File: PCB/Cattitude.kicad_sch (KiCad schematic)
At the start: 15 parts, among them J1 Conn_01x08_Pin, J2 Conn_01x04_Pin, J3 Conn_01x02_Pin, J4 Conn_01x02_Pin, J5 Conn_01x03_Pin, J6 Conn_01x03_Pin, J7 Conn_01x03_Pin, J8 Conn_01x03_Pin, SW2 SW_SPDT, U1 102010551

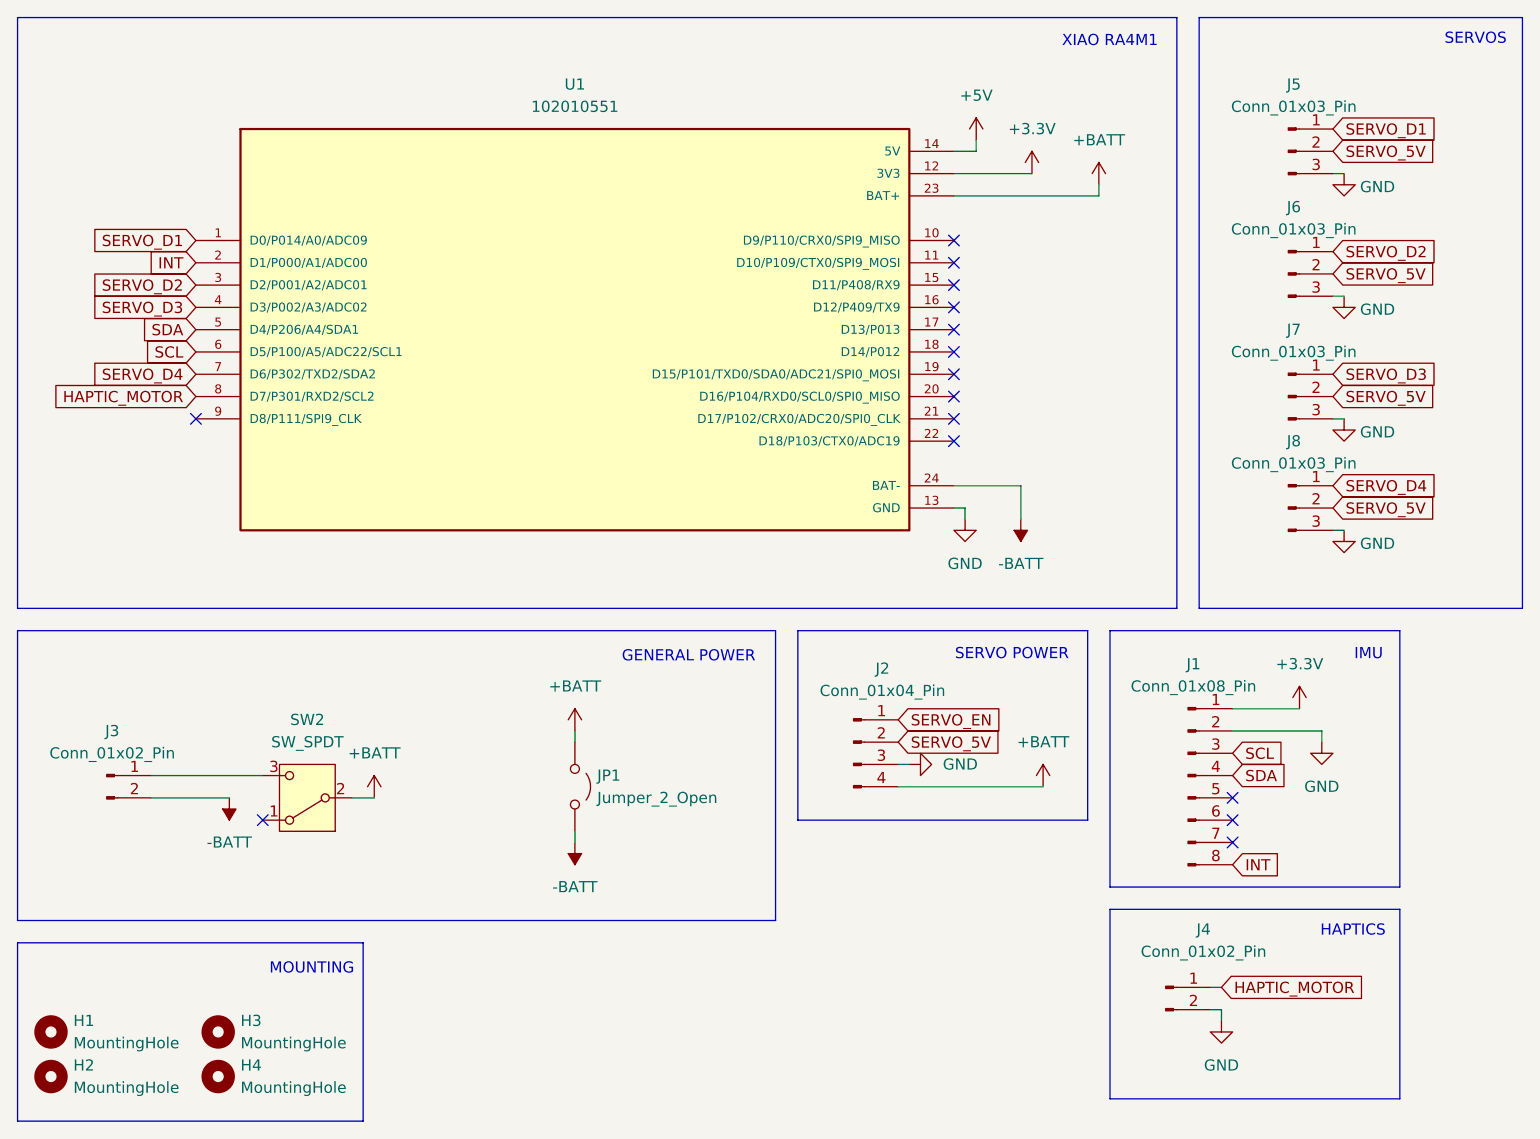
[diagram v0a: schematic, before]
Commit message: PCB Routing done
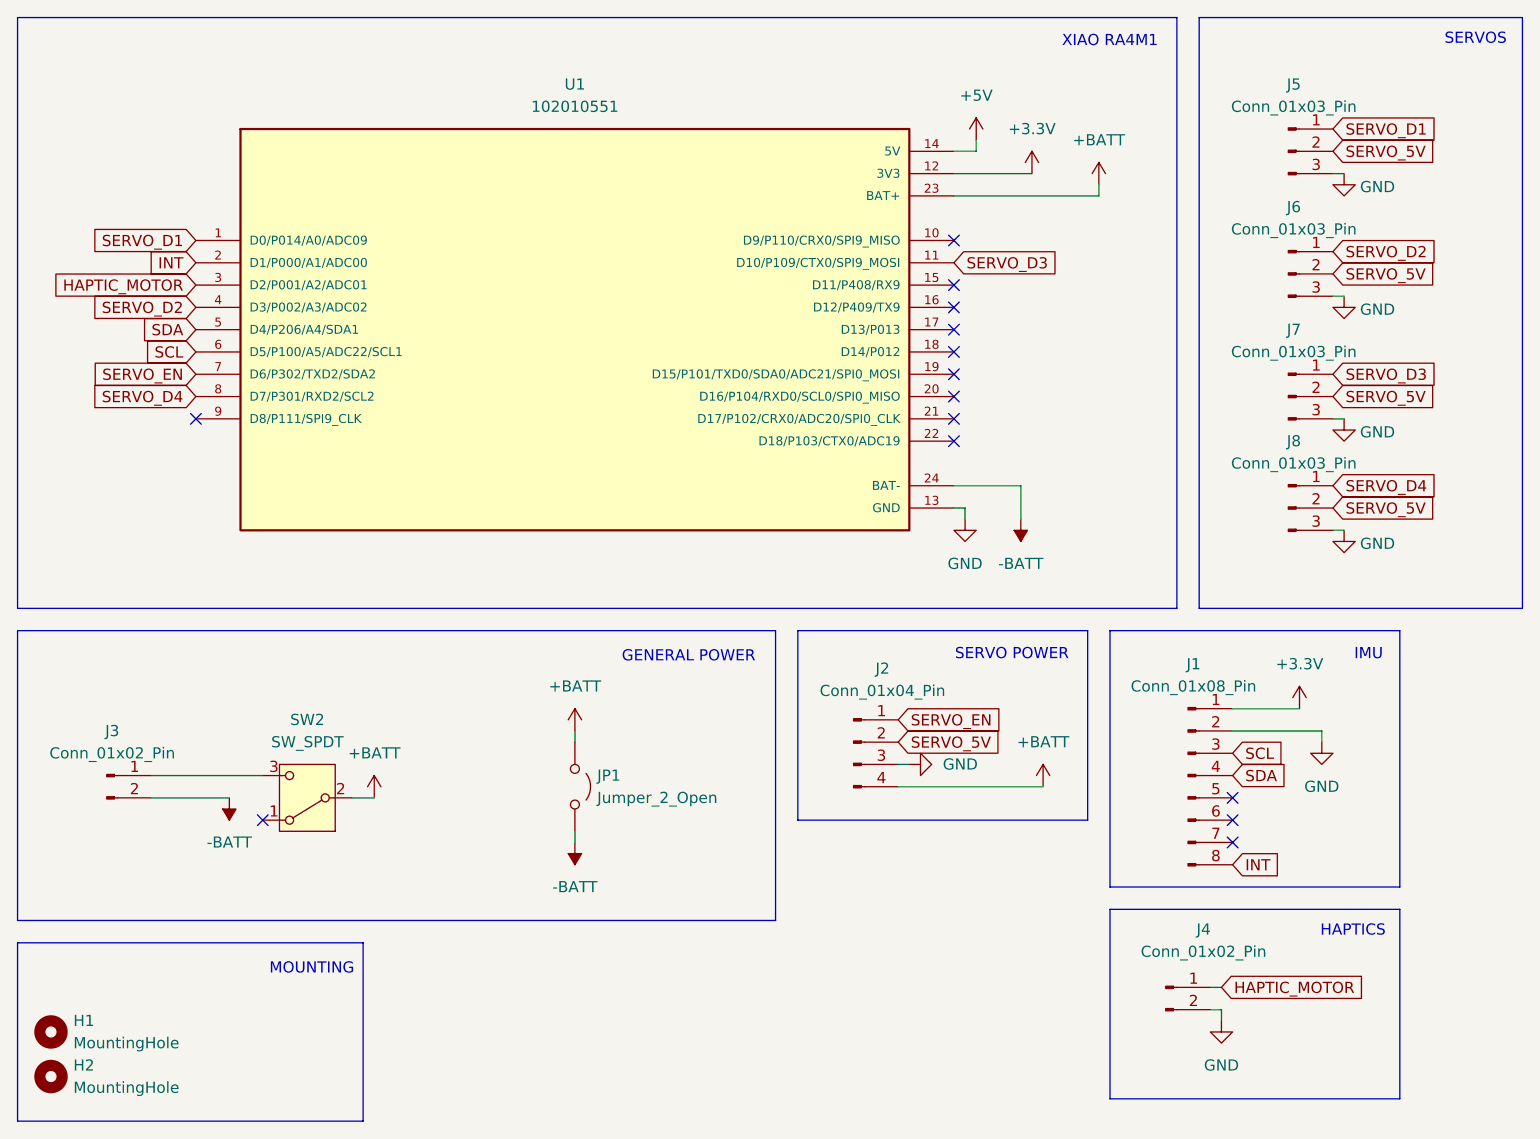
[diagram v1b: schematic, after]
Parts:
- removed H3, H4: MountingHole, MountingHole:MountingHole_2.7mm_M2.5_DIN965_Pad, symbol Mechanical:MountingHole
- J1: footprint Connector_PinHeader_2.54mm:PinHeader_1x08_P2.54mm_Vertical -> CustomParts:MPU 6050
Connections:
- net HAPTIC_MOTOR: now also U1.3 (D2/P001/A2/ADC01); no longer U1.8 (D7/P301/RXD2/SCL2)
- net SERVO_D2: now also U1.4 (D3/P002/A3/ADC02); no longer U1.3 (D2/P001/A2/ADC01)
- net SERVO_D3: now also U1.11 (D10/P109/CTX0/SPI9_MOSI); no longer U1.4 (D3/P002/A3/ADC02)
- net SERVO_D4: now also U1.8 (D7/P301/RXD2/SCL2); no longer U1.7 (D6/P302/TXD2/SDA2)
- net SERVO_EN: now also U1.7 (D6/P302/TXD2/SDA2)
- no-connect marks 15 -> 14
